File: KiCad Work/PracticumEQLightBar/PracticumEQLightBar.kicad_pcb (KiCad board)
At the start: 2 copper layers, 299 x 71.4 mm, 61 parts, among them J2 5V, 4A DC, U1 TEENSY 4.1, U2 TEENSY AUDIO ADAPTER BOARD RE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, U4 SN74AHCT125N

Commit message: Reoriented footprints, larger track width
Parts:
- moved REF** 4.61 mm to (319.4, 138.0)
- moved REF** 4.61 mm to (319.4, 73.0)
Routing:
- net Net-(D29-DO): track 24.8 -> 16.2 mm
- net Net-(D29-CO): track 30.8 -> 24.4 mm
- net 5V DC: track 139.5 -> 138.8 mm
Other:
- board size 299 x 71.4 mm -> 294.6 x 71.4 mm

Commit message: DC jack changed to 2.1mm
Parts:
- C1: value 470u -> 680u
- J2: footprint EQLightBarLibrary:PJ047BH DC Jack -> EQLightBarLibrary:694106301002_1
- moved J2 13.2 mm to (104.2, 69.7)
- moved D34 0.73 mm to (252.6, 123.5)
- moved D30 0.73 mm to (297.1, 123.5)
- moved D31 0.73 mm to (288.2, 123.5)
- moved D32 0.73 mm to (279.3, 123.5)
- moved D33 0.73 mm to (261.5, 123.5)
- moved D35 0.73 mm to (234.8, 123.5)
- moved D36 0.73 mm to (225.9, 123.5)
- moved D37 0.73 mm to (217.1, 123.5)
- moved D38 0.73 mm to (199.3, 123.5)
- moved D39 0.73 mm to (190.4, 123.5)
- moved D40 0.73 mm to (172.6, 123.5)
- moved D41 0.73 mm to (163.7, 123.5)
- moved D42 0.73 mm to (154.8, 123.5)
- moved D43 0.73 mm to (137.0, 123.5)
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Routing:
- net 5V DC: track 138.8 -> 153.3 mm
- net Net-(D29-DO): track 16.2 -> 8.48 mm
- net Net-(D29-CO): track 24.4 -> 18.1 mm

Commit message: Rerouting, smaller board size, keys enclosure sizing
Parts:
- removed U2: TEENSY AUDIO ADAPTER BOARD REV D, EQLightBarLibrary:MODULE_DEV-15845
- moved C2 65.6 mm to (101.6, 90.2)
- moved U4 11.4 mm to (76.2, 108.1)
- moved REF** 10.3 mm to (40.0, 78.0)
- moved REF** 9.00 mm to (40.0, 138.0)
- moved U1 8.89 mm to (38.1, 91.4)
- moved J2 5.39 mm to (108.0, 73.5)
- moved REF** 5.00 mm to (319.4, 78.0)
- moved C1 2.01 mm to (52.6, 119.4)
- moved R1 1.27 mm to (43.2, 115.6)
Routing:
- net Net-(D1-CI): track 57.7 -> 71.3 mm
- net Net-(U4-1Y): track 27.6 -> 40.3 mm
- net Net-(D29-DO): track 8.48 -> 16.0 mm
- net Net-(D29-CO): track 18.1 -> 24.2 mm
- net 5V DC: track 153.3 -> 157.2 mm
- net /3.3V DATA: track 5.08 -> 7.40 mm
- net Net-(D1-DI): track 17.7 -> 19.0 mm
- net /CLOCK: track 7.18 -> 6.13 mm
- net unconnected-(U1-TX7-Pad29): track 0.00 -> 0.53 mm
- net unconnected-(U1-OUT1B-Pad32): track 0.53 -> 0.00 mm
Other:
- board size 294.6 x 71.4 mm -> 285.8 x 66.4 mm

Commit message: Added test points
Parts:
- added TP1: TestPoint, TestPoint:TestPoint_Pad_1.0x1.0mm, F.Cu at (54.6, 76.2)
- added TP2: TestPoint, TestPoint:TestPoint_Pad_1.0x1.0mm, F.Cu at (59.1, 119.4)
- added TP3: TestPoint, TestPoint:TestPoint_Pad_1.0x1.0mm, F.Cu at (110.5, 89.5)
- added TP4: TestPoint, TestPoint:TestPoint_Pad_1.0x1.0mm, F.Cu at (125.7, 89.5)
- moved C2 58.2 mm to (44.5, 78.7), turned to 0 degrees
- moved J2 6.35 mm to (114.3, 73.5)
- moved REF** 0.82 mm to (39.4, 77.5)
- moved REF** 0.76 mm to (39.4, 138.4)
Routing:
- net 5V DC: track 157.2 -> 810.2 mm
- net /3.3V DATA: track 7.40 -> 6.13 mm
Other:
- board text removed: "~49 keys, mirrored in light~"

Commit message: added horrible power bus for LEDs
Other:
- board text added: "TO DO: GND stitching"
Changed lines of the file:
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@@
 			(at 0 -2.7 0)
 			(layer "F.SilkS")
+			(hide yes)
 			(effects
 				(font
@@
 			(at 0 -2.7 0)
 			(layer "F.SilkS")
+			(hide yes)
 			(effects
 				(font
@@
 			(at 0 -2.7 0)
 			(layer "F.SilkS")
+			(hide yes)
 			(effects
 				(font
@@
 			(at 0 -2.7 0)
 			(layer "F.SilkS")
+			(hide yes)
 			(effects
 				(font
@@
 			(at 0 -2.7 0)
 			(layer "F.SilkS")
+			(hide yes)
 			(effects
 				(font
@@
 		)
 	)
+	(gr_text "TO DO: GND stitching"
+		(at 46.355 149.86 0)
+		(layer "Cmts.User")
+		(effects
+			(font
+				(size 1 1)
+				(thickness 0.2)
+				(bold yes)
+			)
+			(justify bottom)
+		)
+	)
 	(segment
 		(start 63.79 130.72)
@@
 		(fill yes
 			(thermal_gap 0.5)
-			(thermal_bridge_width 0.5)
+			(thermal_bridge_width 2)
 			(island_removal_mode 1)
 			(island_area_min 10)
@@
 		(fill yes
 			(thermal_gap 0.5)
-			(thermal_bridge_width 0.5)
+			(thermal_bridge_width 2)
 		)
 		(polygon

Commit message: final PCB layout
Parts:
- added C3: 33u, Capacitor_THT:CP_Radial_D4.0mm_P2.00mm, F.Cu at (113.0, 92.1)
- added C4: 33u, Capacitor_THT:CP_Radial_D4.0mm_P2.00mm, F.Cu at (158.8, 102.9)
- added C5: 0.5u, Capacitor_THT:C_Disc_D4.7mm_W2.5mm_P5.00mm, F.Cu at (158.8, 94.0)
- added C6: 0.1u, Capacitor_THT:C_Disc_D4.7mm_W2.5mm_P5.00mm, F.Cu at (149.9, 99.1)
- added C7: 0.1u, Capacitor_THT:C_Disc_D4.7mm_W2.5mm_P5.00mm, F.Cu at (69.2, 112.4)
- added J1: Conn_01x02_Socket, Connector_PinHeader_2.54mm:PinHeader_1x02_P2.54mm_Vertical, F.Cu at (165.1, 105.4)
- added J3: Conn_01x02_Socket, Connector_PinHeader_2.54mm:PinHeader_1x02_P2.54mm_Vertical, F.Cu at (125.7, 104.8)
- added R2: 330, Resistor_THT:R_Axial_DIN0207_L6.3mm_D2.5mm_P7.62mm_Horizontal, F.Cu at (143.5, 94.0)
- added REF**: MountingHole_2.2mm_M2_ISO7380_Pad, MountingHole:MountingHole_2.2mm_M2_ISO7380_Pad, F.Cu at (177.0, 112.0)
- added RV2: R_Potentiometer, EQLightBarLibrary:PTV09A4030FA104 Pot 100k, F.Cu at (137.8, 102.2)
- added TP5: TestPoint, Connector_PinHeader_2.54mm:PinHeader_1x01_P2.54mm_Vertical, F.Cu at (43.2, 116.8)
- added TP6: TestPoint, Connector_PinHeader_2.54mm:PinHeader_1x01_P2.54mm_Vertical, F.Cu at (39.4, 116.8)
- added U3: LM386, Package_DIP:DIP-8_W7.62mm, F.Cu at (147.3, 110.5)
- moved TP1 56.9 mm to (109.2, 92.1), turned to 0 degrees
- moved REF** 42.6 mm to (144.0, 79.0)
- moved TP3 35.0 mm to (144.1, 99.1)
- moved REF** 34.0 mm to (319.0, 112.0)
- moved U4 21.0 mm to (55.2, 108.4)
- moved C2 11.3 mm to (41.3, 89.6), turned to -90 degrees
- moved TP2 5.85 mm to (54.6, 115.6)
- moved R1 4.44 mm to (43.2, 120.0)
- moved C1 3.14 mm to (49.5, 118.7), turned to -90 degrees
- moved REF** 1.57 mm to (39.0, 79.0)
- moved REF** 1.09 mm to (319.0, 139.0)
- moved REF** 0.68 mm to (39.0, 139.0)
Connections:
- net /3.3V DATA renamed SDA
- net /CLOCK renamed SCL
- net 5V DC renamed +5V
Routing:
- net +5V: track 810.2 -> 847.9 mm
- net Net-(D1-CI): track 71.3 -> 49.3 mm
- net Net-(U3-+): track 0.00 -> 20.6 mm
- net SCL: track 6.13 -> 25.7 mm
- net Net-(U4-1Y): track 40.3 -> 24.5 mm
- net SDA: track 6.13 -> 20.6 mm
- net Net-(C4-Pad1): track 0.00 -> 12.7 mm
- net Net-(J3-Pin_2): track 0.00 -> 7.02 mm
- net Net-(J1-Pin_2): track 0.00 -> 4.35 mm
- net Net-(C5-Pad2): track 0.00 -> 2.62 mm
- net Net-(D1-DI): track 19.0 -> 17.1 mm
- net GND: vias 0 -> 148
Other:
- board size 285.8 x 66.4 mm -> 286 x 66 mm
- board text added: "${TITLE} v${REVISION} 2025-11-20 Team 3, ECE 411, PSU"
- board text removed: "TO DO: GND stitching"
- board text removed: "The GND/5V edge of the board should probably line up with the left side of the PCB so that both the built-in aux jack and micro-usb port can be flush with the enclosure"

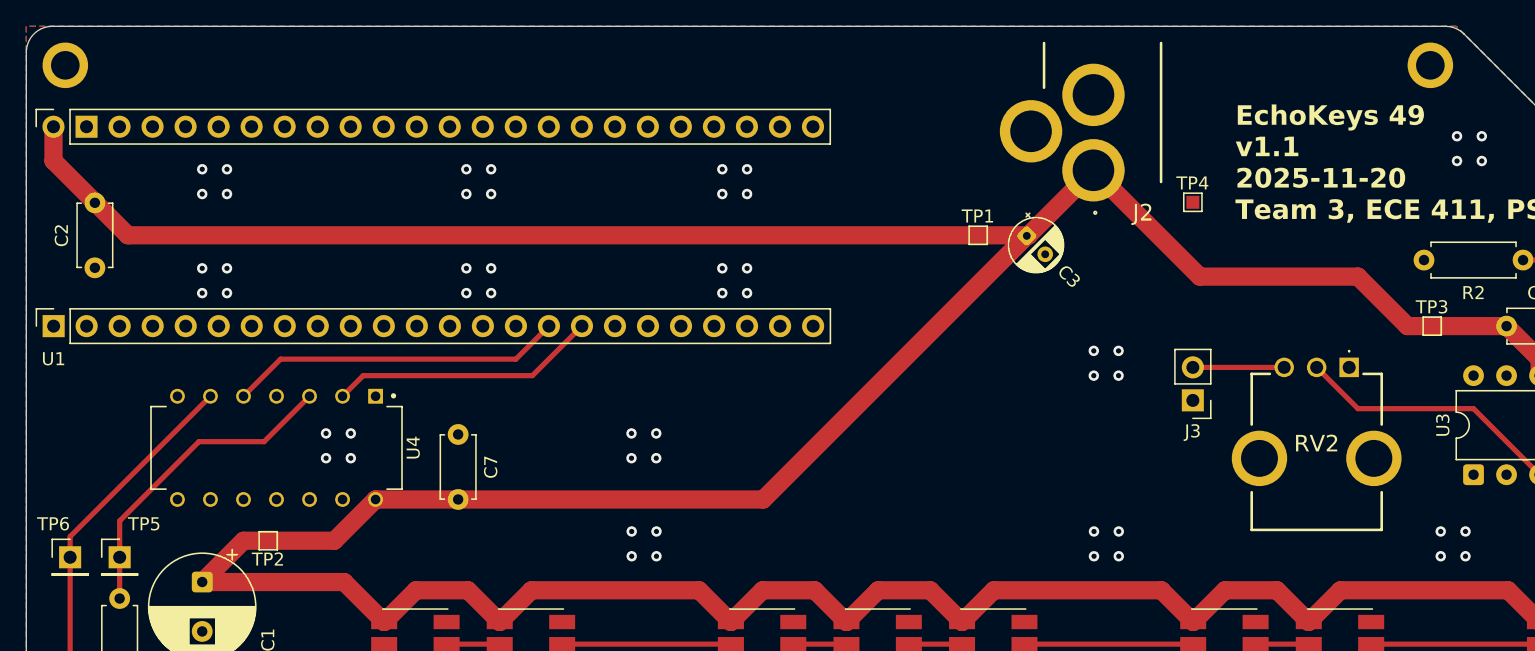
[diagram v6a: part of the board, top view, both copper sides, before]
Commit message: Drawing sheets updated with final PCB design
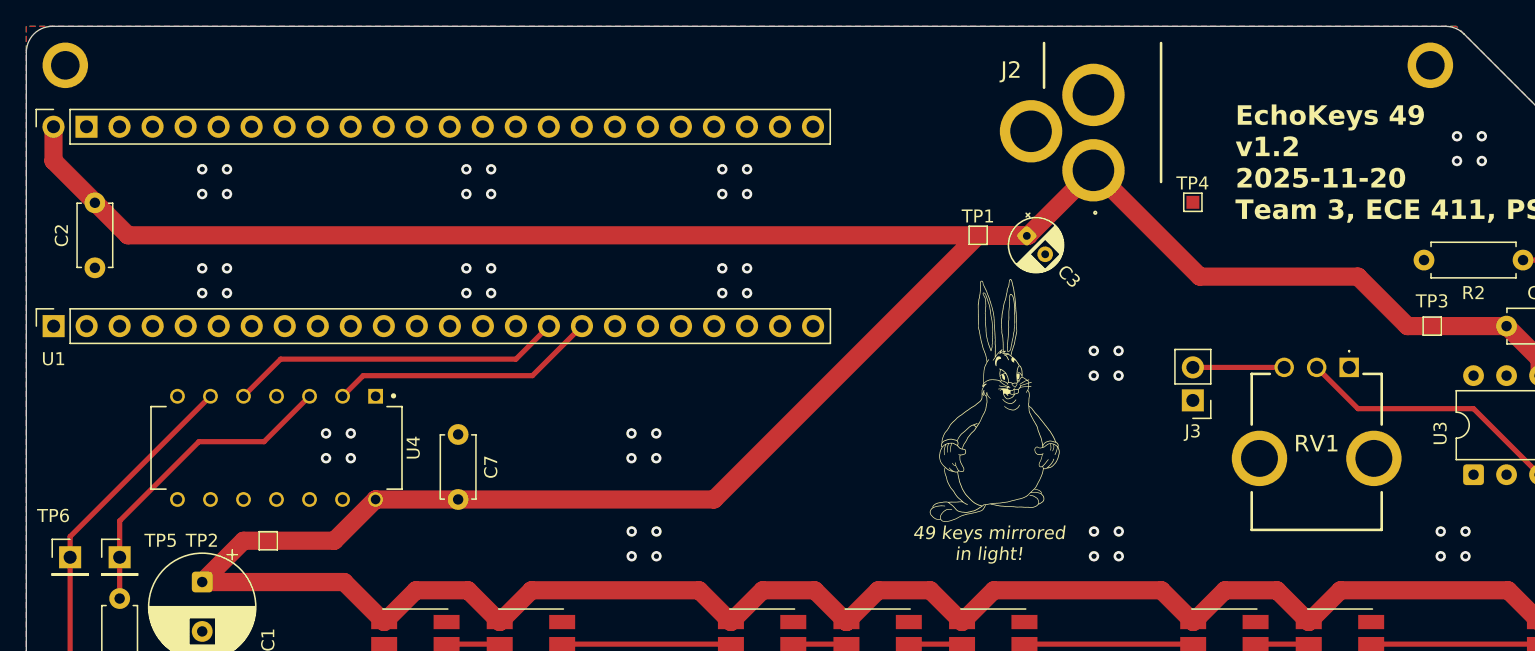
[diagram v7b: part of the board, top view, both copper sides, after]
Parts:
- added REF**: Big Chungus, EQLightBarLibrary:Big Chungus, F.Cu at (110.5, 107.4)
- renumbered RV2 to RV1
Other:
- board text added: "49 keys mirrored in light!"
